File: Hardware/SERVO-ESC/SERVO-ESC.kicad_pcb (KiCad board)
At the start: 4 copper layers, 39.4 x 32.3 mm, 43 parts, among them IC1 DRV8876PWPR, IC2 TMP102xxDRL, IC3 INA236AIDDFR, IC4 MT6816CT, IC5 AP2112K, J1 Conn_01x04_Pin, J2 Conn_01x04_Pin, J3 Conn_01x05_Pin, J5 +, J6 -, U1 STM32F301C8Tx, Y1 25MHZ

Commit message: New PCB Files
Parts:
- removed the C13 at (69.5, 26.0)
- removed the C15 at (63.0, 43.9)
- removed C16: 10nF, Capacitor_SMD:C_0402_1005Metric
- removed FB1: 120, Inductor_SMD:L_0603_1608Metric
- removed the IC4 at (71.2, 22.7)
- removed J3: Conn_01x05_Pin, Connector_JST:JST_SH_SM05B-SRSS-TB_1x05-1MP_P1.00mm_Horizontal
- added C12: 1uF, Capacitor_SMD:C_0402_1005Metric, F.Cu at (66.4, 41.6)
- added R1: 10k, Resistor_SMD:R_0402_1005Metric, F.Cu at (70.9, 33.2)
- added R12: 4.7k, Resistor_SMD:R_0402_1005Metric, F.Cu at (58.6, 34.6)
- added R13: 4.7k, Resistor_SMD:R_0402_1005Metric, F.Cu at (61.0, 40.4)
- added R7: 1k, Resistor_SMD:R_0402_1005Metric, F.Cu at (61.4, 44.5)
- D1: value 6V -> LED; footprint Diode_SMD:D_0402_1005Metric -> LED_SMD:LED_0603_1608Metric
- J4: renamed from MAG; footprint Connector_PinSocket_1.00mm:PinSocket_1x05_P1.00mm_Vertical -> Connector_PinHeader_2.00mm:PinHeader_1x05_P2.00mm_Vertical
- LED1: renamed from RGB; value (none) -> ~
- moved D1 20.0 mm to (61.3, 42.7), turned to 180 degrees
- moved J4 8.16 mm to (76.8, 48.0), turned to -90 degrees
- moved C5 1.67 mm to (68.8, 32.4)
- moved C2 1.03 mm to (66.5, 36.1), turned to 90 degrees
- moved C1 0.68 mm to (69.3, 33.7)
- moved LED1 0.63 mm to (60.1, 44.1)
- moved R3 0.51 mm to (64.3, 47.2)
- moved R4 0.50 mm to (64.3, 46.0)
- moved R2 0.41 mm to (64.3, 48.5)
- moved J2 0.23 mm to (64.6, 32.6)
- moved C17 0.22 mm to (61.7, 35.7)
- moved C11 0.20 mm to (81.5, 33.8)
- moved J1 0.20 mm to (51.4, 44.1)
- moved IC4 0.19 mm to (61.0, 37.5)
- moved C10 0.10 mm to (82.8, 36.4)
- renumbered C7 to C1, C3 to C10, C4 to C11, C5 to C13, C6 to C14, C12 to C15, C14 to C17, C8 to C2, C9 to C3, C10 to C4, C11 to C5, C17 to C6, C1 to C7, C18 to C8, C2 to C9, IC5 to IC1, IC1 to IC2, IC2 to IC4, IC3 to IC5, R2 to R10, R1 to R11, R7 to R2, R6 to R3, R5 to R4, R8 to R5, R9 to R6, R3 to R8, R4 to R9
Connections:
- net I2C-SCL-2 renamed UART-TX
- net I2C-SDA-2 renamed UART-RX
- D1 pad 1: GND -> Net-(D1-K)
- J2 pad 4: 3.3V -> +3.3V
- R5 pad 2: I2C-SDA-1 -> I2C-SCL-1
- R6 pad 2: I2C-SCL-1 -> I2C-SDA-1
- U1 pad 26: MAG-MOSI -> MAG-SCLK
- U1 pad 28: MAG-SCLK -> MAG-MOSI
- U1 pad 41: I2C-SDA-1 -> unconnected-(U1-PB5-Pad41)
- U1 pad 43: unconnected-(U1-PB7-Pad43) -> I2C-SDA-1
- U1 pad 44: unconnected-(U1-BOOT0-Pad44) -> Net-(U1-BOOT0)
- U1 pad 45: unconnected-(U1-PB8-Pad45) -> INA236-INT
- U1 pad 9: +3.3VA -> +3.3V
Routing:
- net INA236-INT: track 0.76 -> 17.9 mm, vias 1 -> 2
- net MAG-SCLK: track 21.3 -> 10.2 mm, vias 2 -> 1
- net GND: track 30.0 -> 21.8 mm, vias 37 -> 46
- net +3.3VA: track 6.55 -> 0.00 mm
- net MAG-MISO: track 17.6 -> 11.7 mm, vias 2 -> 1
- net +SV: track 2.24 -> 5.63 mm
- net I2C-SCL-1: track 25.2 -> 22.2 mm
- net +3.3V: track 34.4 -> 31.9 mm, vias 24 -> 22
- net Net-(D1-K): track 0.00 -> 1.91 mm
- net Net-(U1-BOOT0): track 0.00 -> 1.77 mm
- net +7V: track 53.1 -> 52.0 mm
- net TMP102-INT: track 17.3 -> 16.3 mm, vias 3 -> 2
- net MAG-MOSI: track 14.1 -> 13.4 mm, vias 2 -> 1
- net I2C-SDA-1: track 20.3 -> 19.7 mm
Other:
- board size 39.4 x 32.3 mm -> 38.4 x 18.4 mm

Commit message: New Commit
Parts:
- added C16: 10nF, Capacitor_SMD:C_0402_1005Metric, F.Cu at (115.8, 38.4)
- added D2: TVS 6V, Diode_SMD:D_0402_1005Metric, F.Cu at (115.8, 40.6)
- added J3: MAG, Connector_PinSocket_2.00mm:PinSocket_1x04_P2.00mm_Vertical, F.Cu at (116.8, 43.0)
- added R14: 4.7k, Resistor_SMD:R_0402_1005Metric, F.Cu at (124.2, 38.4)
- added R15: 4.7k, Resistor_SMD:R_0402_1005Metric, F.Cu at (124.2, 40.4)
- added REF**: L_0603_1608Metric, Inductor_SMD:L_0603_1608Metric, F.Cu at (66.2, 42.0)
- added U2: MT6701CT, Package_SO:SO-8_3.9x4.9mm_P1.27mm, F.Cu at (120.0, 39.6)
- J4: value Conn_01x05 -> Conn_01x04_Pin; footprint Connector_PinHeader_2.00mm:PinHeader_1x05_P2.00mm_Vertical -> Connector_PinSocket_2.54mm:PinSocket_1x04_P2.54mm_Vertical
- moved J4 7.87 mm to (68.9, 48.0), turned to 90 degrees
- moved C12 2.69 mm to (64.5, 43.5)
- renumbered J5 to +, J6 to -, C17 to C16
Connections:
- J4 pad 1: +3.3V -> I2C-SDA-3
- J4 pad 2: GND -> I2C-SCL-3
- J4 pad 3: MAG-SCLK -> GND
- J4 pad 4: MAG-MISO -> +3.3V
- R8 pad 2: GND -> +3.3V
- U1 pad 26: MAG-SCLK -> unconnected-(U1-PB13-Pad26)
- U1 pad 27: MAG-MISO -> HBRIDGE-IN2
- U1 pad 28: MAG-MOSI -> HBRIDGE-IN1
- U1 pad 29: HBRIDGE-IN2 -> I2C-SCL-3
- U1 pad 32: HBRIDGE-IN1 -> unconnected-(U1-PA11-Pad32)
- U1 pad 41: unconnected-(U1-PB5-Pad41) -> I2C-SDA-3
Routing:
- net I2C-SDA-3: track 0.00 -> 20.2 mm, vias 0 -> 1
- net I2C-SCL-3: track 0.00 -> 19.7 mm, vias 0 -> 1
- net +3.3V: track 31.9 -> 49.2 mm, vias 22 -> 25
- net MAG-MOSI: track 13.4 -> 0.00 mm, vias 1 -> 0
- net MAG-MISO: track 11.7 -> 0.00 mm, vias 1 -> 0
- net GND: track 21.8 -> 32.5 mm
- net MAG-SCLK: track 10.2 -> 0.00 mm, vias 1 -> 0
- net HBRIDGE-IN1: track 8.03 -> 6.56 mm
- net HBRIDGE-VREF: track 18.7 -> 17.5 mm
- net HBRIDGE-IN2: track 10.2 -> 9.24 mm
- net RGB-LED-RED: track 12.4 -> 11.7 mm
- net +7V: vias 9 -> 8
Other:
- board size 38.4 x 18.4 mm -> 75 x 18.4 mm
- board text added: "Servo Electronic Speed Controller Made by Chinedu Okpala 2/28/26"

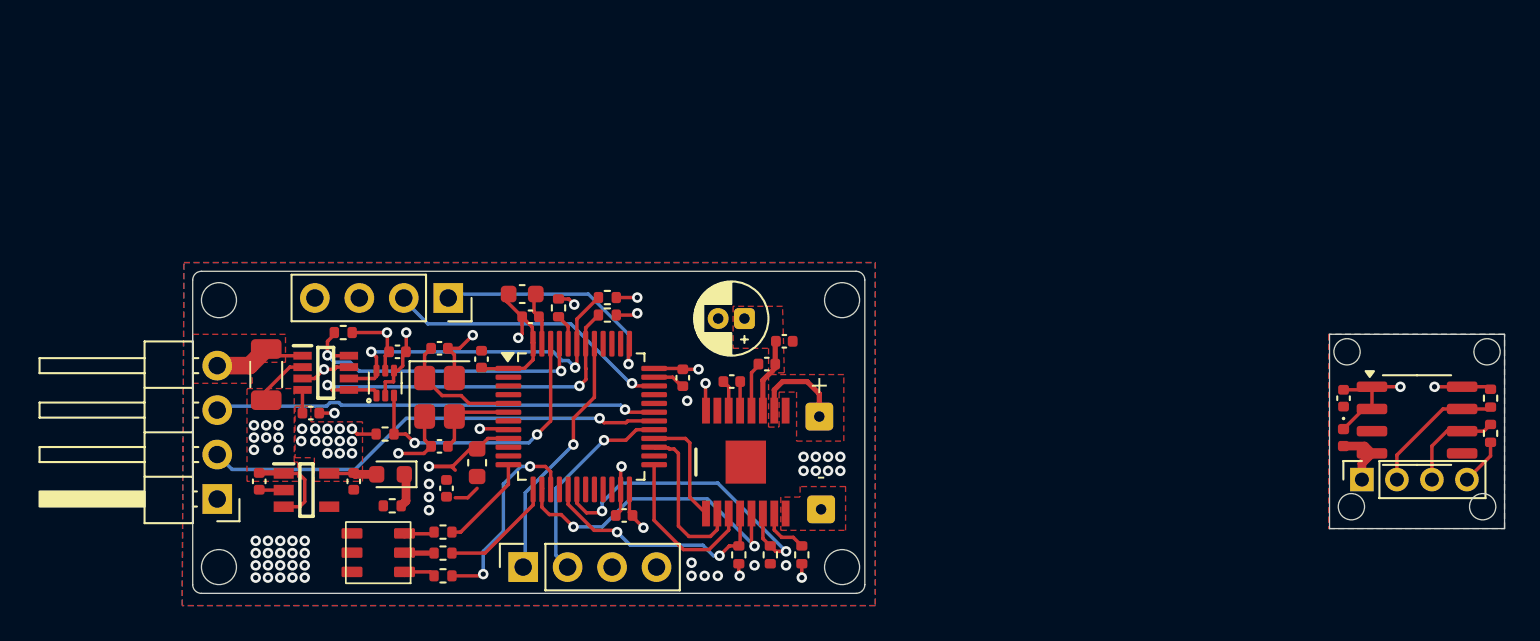
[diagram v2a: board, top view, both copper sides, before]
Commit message: New board files (messed up gnd via)
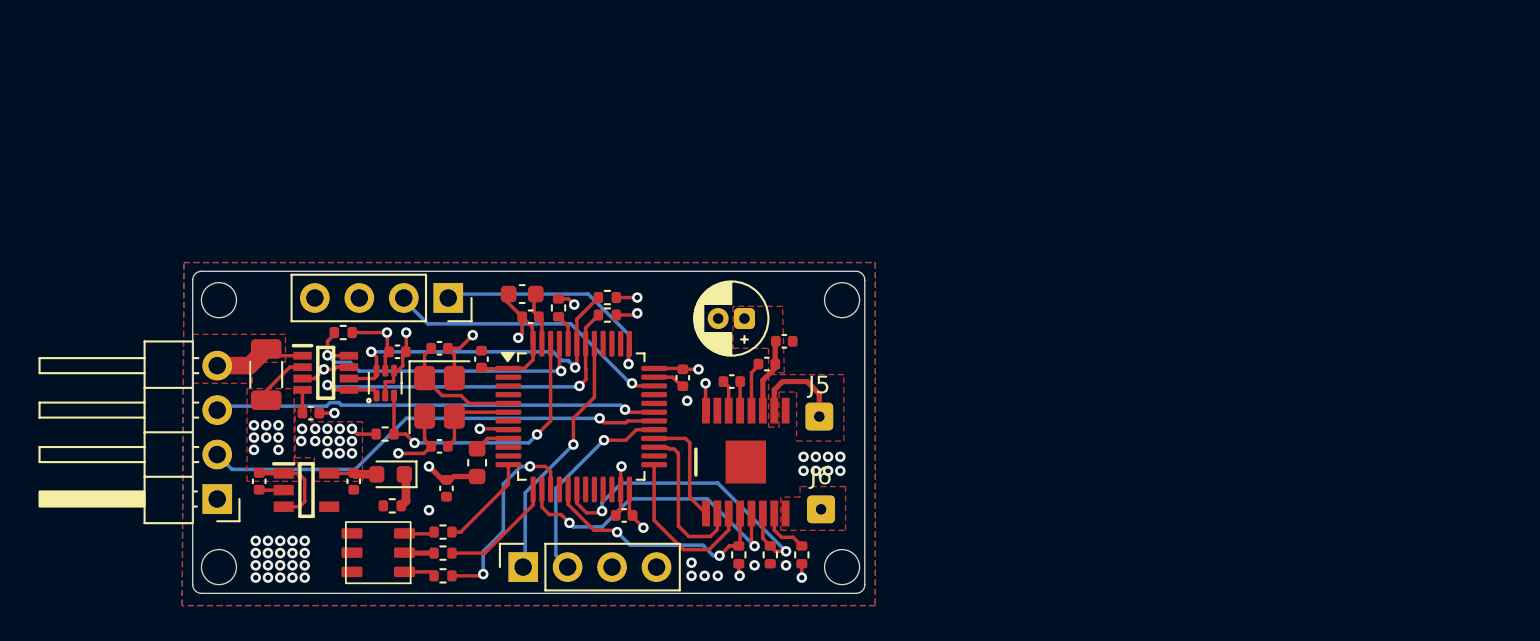
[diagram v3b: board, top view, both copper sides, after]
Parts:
- removed the C16 at (115.8, 38.4)
- removed D2: TVS 6V, Diode_SMD:D_0402_1005Metric
- removed J3: MAG, Connector_PinSocket_2.00mm:PinSocket_1x04_P2.00mm_Vertical
- removed R14, R15: 4.7k, Resistor_SMD:R_0402_1005Metric
- removed REF**: L_0603_1608Metric, Inductor_SMD:L_0603_1608Metric
- removed U2: MT6701CT, Package_SO:SO-8_3.9x4.9mm_P1.27mm
- added FB1: FerriteBead, Inductor_SMD:L_0603_1608Metric, F.Cu at (66.2, 42.0)
- renumbered + to J5, - to J6
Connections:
- U1 pad 9: +3.3V -> +3.3VA
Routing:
- net +3.3V: track 49.2 -> 32.9 mm, vias 25 -> 23
- net I2C-SCL-3: track 19.7 -> 11.8 mm
- net I2C-SDA-3: track 20.2 -> 14.4 mm
- net GND: track 32.5 -> 27.5 mm, vias 46 -> 44
- net +3.3VA: track 0.00 -> 3.11 mm
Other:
- board size 75 x 18.4 mm -> 38.4 x 18.4 mm
